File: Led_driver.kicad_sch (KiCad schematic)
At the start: 10 parts, among them IC2 A6214KLKTR-T

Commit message: finished boarD
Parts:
- C23: LCSC (none) -> C96446
- C24: LCSC (none) -> C19666
- C25: LCSC (none) -> C15849
- C26, C27: LCSC (none) -> C14663
- D1: LCSC (none) -> C8678
- IC2: LCSC (none) -> C146400
- L2: LCSC (none) -> C5127262
- R13: LCSC (none) -> C23175
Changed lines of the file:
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@@
+			)
+		)
+		(property "LCSC" "C15849"
+			(at 94.742 93.726 0)
+			(effects
+				(font
+					(size 1.27 1.27)
+				)
+				(hide yes)
 			)
 		)
@@
 		)
 		(property "Description" "Unpolarized capacitor, small symbol"
+			(at 161.29 93.98 0)
+			(effects
+				(font
+					(size 1.27 1.27)
+				)
+				(hide yes)
+			)
+		)
+		(property "LCSC" "C14663"
 			(at 161.29 93.98 0)
 			(effects
@@
 			)
 		)
+		(property "LCSC" "C23175"
+			(at 94.488 78.74 0)
+			(effects
+				(font
+					(size 1.27 1.27)
+				)
+				(hide yes)
+			)
+		)
 		(pin "2"
 		)
@@
 		(property "Description" "Unpolarized capacitor, small symbol"
 			(at 76.2 67.31 0)
+			(effects
+				(font
+					(size 1.27 1.27)
+				)
+				(hide yes)
+			)
+		)
+		(property "LCSC" "C96446"
+			(at 75.946 65.786 0)
 			(effects
 				(font
@@
 			)
 		)
+		(property "LCSC" ""
+			(at 161.29 85.09 0)
+			(effects
+				(font
+					(size 1.27 1.27)
+				)
+			)
+		)
 		(pin "2"
 		)
@@
 			)
 		)
+		(property "LCSC" "C146400"
+			(at 104.14 80.01 0)
+			(effects
+				(font
+					(size 1.27 1.27)
+				)
+				(hide yes)
+			)
+		)
 		(pin "8"
 		)
@@
 		)
 		(property "Description" "Unpolarized capacitor, small symbol"
+			(at 143.51 77.47 0)
+			(effects
+				(font
+					(size 1.27 1.27)
+				)
+				(hide yes)
+			)
+		)
+		(property "LCSC" "C14663"
 			(at 143.51 77.47 0)
 			(effects
@@
 			)
 		)
+		(property "LCSC" "C8678"
+			(at 152.4 77.47 0)
+			(effects
+				(font
+					(size 1.27 1.27)
+				)
+				(hide yes)
+			)
+		)
 		(pin "1"
 		)
@@
 			)
 		)
+		(property "LCSC" "C5127262"
+			(at 157.48 73.66 0)
+			(effects
+				(font
+					(size 1.27 1.27)
+				)
+				(hide yes)
+			)
+		)
 		(pin "2"
 		)
@@
 			(effects
 				(font
+					(size 1.27 1.27)
+				)
+				(hide yes)
+			)
+		)
+		(property "LCSC" "C19666"
+			(at 85.09 66.04 0)
+			(effects
+				(font

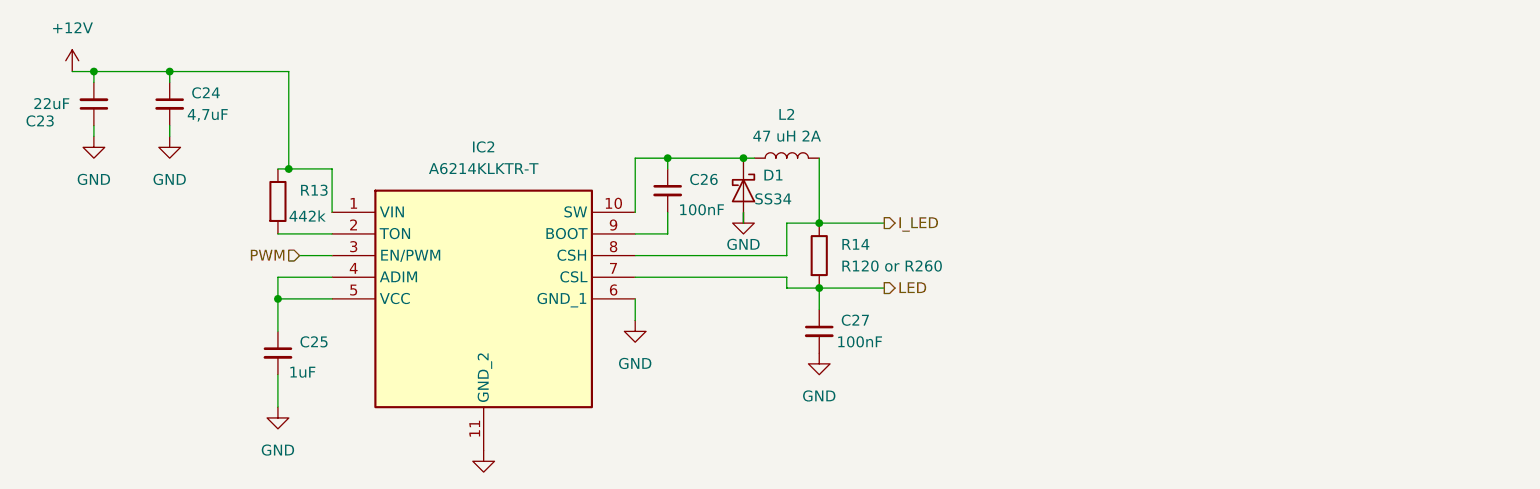
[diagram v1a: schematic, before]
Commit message: Added current sense amplifier, reduced one ADC, changed elec cap to tantals, to review
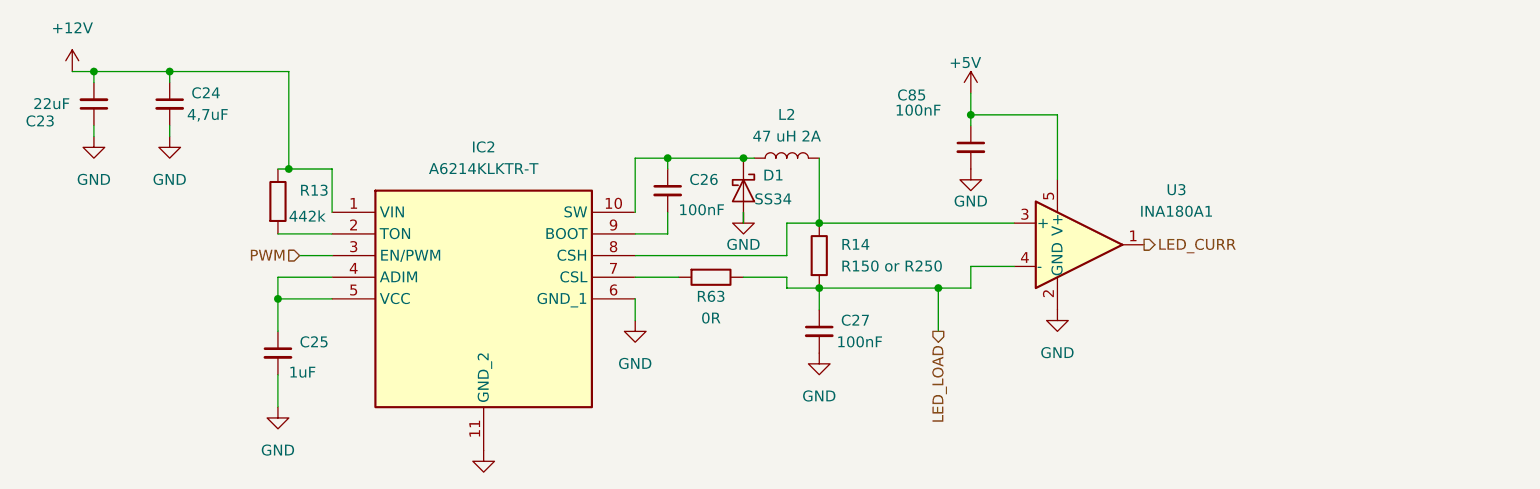
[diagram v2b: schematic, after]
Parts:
- added C85: 100nF, Capacitor_SMD:C_0603_1608Metric_Pad1.08x0.95mm_HandSolder, symbol Device:C_Small
- added R63: 0R, Capacitor_SMD:C_0402_1005Metric_Pad0.74x0.62mm_HandSolder, symbol PCM_SL_Resistors:Resistor
- added U3: INA180A1, Package_TO_SOT_SMD:SOT-23-5, symbol Amplifier_Current:INA180A1
- R14: value R120 or R260 -> R150 or R250
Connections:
- net GND: now also C85.2, U3.2 (GND)
- net I_LED: no longer names the net of IC2.8 (CSH), L2.2, R14.2
- net I_LED: now also U3.3 (+)
- net LED renamed LED_LOAD
- net LED_LOAD: now also R63.2, U3.4 (-); no longer IC2.7 (CSL)
- new net: IC2.7 (CSL), R63.1
- new net +5V: C85.1, U3.5 (V+)
- new net LED_CURR: U3.1

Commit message: Added low pass filters at current sense amp outputs and pull ups on cs pins, DRC done
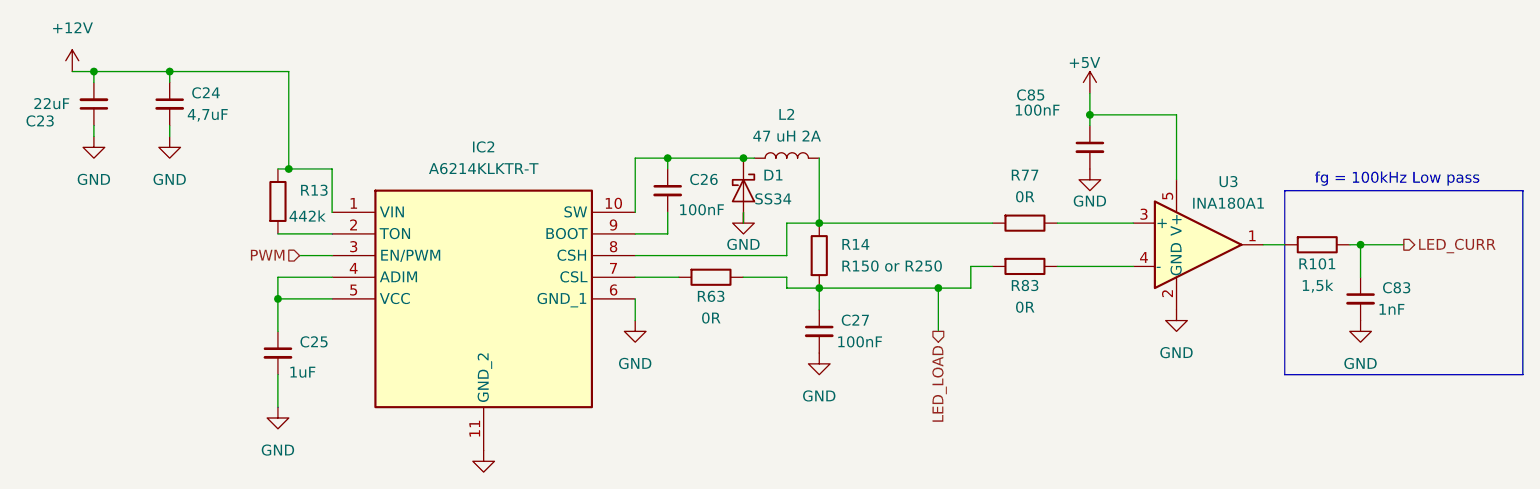
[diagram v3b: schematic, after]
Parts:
- added C83: 1nF, Capacitor_SMD:C_0402_1005Metric_Pad0.74x0.62mm_HandSolder, symbol Device:C_Small
- added R101: 1,5k, Resistor_SMD:R_0402_1005Metric_Pad0.72x0.64mm_HandSolder, symbol PCM_SL_Resistors:Resistor
- added R77, R83: 0R, Resistor_SMD:R_0402_1005Metric_Pad0.72x0.64mm_HandSolder, symbol PCM_SL_Resistors:Resistor
- R63: footprint Capacitor_SMD:C_0402_1005Metric_Pad0.74x0.62mm_HandSolder -> Resistor_SMD:R_0402_1005Metric_Pad0.72x0.64mm_HandSolder
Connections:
- net GND: now also C83.2
- net LED_CURR: now also C83.1, R101.2; no longer U3.1
- net LED_LOAD: now also R83.1; no longer U3.4 (-)
- net at IC2.8 (CSH), L2.2, R14.2: now also R77.1; no longer U3.3 (+)
- new net: R101.1, U3.1
- new net: R77.2, U3.3 (+)
- new net: R83.2, U3.4 (-)
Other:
- note added: "fg = 100kHz Low pass"
- moved on the sheet: C85, U3
